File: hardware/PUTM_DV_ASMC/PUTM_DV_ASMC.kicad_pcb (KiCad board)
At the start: 4 copper layers, 100 x 60 mm, 182 parts, among them IC1 BTS722204ESAXUMA1, IC2 BTS722204ESAXUMA1, J1 FTSH-107-01-L-D-K, J2 IPBS-110-01-XX-D-GP, J3 Conn_01x01_Socket, J4 74650073R, Q1 30V/5A, Q2 BUK6D210, Q3 BUK6D210, Q4 BUK6D210, Q5 BUK6D210, T1 TP_VCC, T2 TP_+5V, T3 TP_+3V3, T4 TP_GND, T5 TP_GND, T6 TP_VCC, T7 TP_GND, T8 TP_+5V, T9 TP_GND, U1 LM4040C33FTA, U2 STM32G484RETx, U3 LM1117-3.3, U4 TPS54202HDDCR, U5 ADM3057ExRW, U6 ADM3057ExRW, U7 TLP291-4, Y1 ATX-11-F-32.000MHZ-F05-T

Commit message: make function section
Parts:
- moved TP6 238.4 mm to (276.2, 70.0)
- moved TP7 238.4 mm to (276.2, 73.0)
- moved TP1 219.3 mm to (268.9, 71.8)
- moved C66 156.9 mm to (178.9, 124.3), turned to 90 degrees
- moved D1 155.3 mm to (185.3, 114.2)
- moved D2 154.9 mm to (185.3, 115.9)
- moved D3 154.6 mm to (185.3, 117.7)
- moved D4 154.2 mm to (185.3, 119.5)
- moved C1 153.8 mm to (170.8, 125.2), turned to 180 degrees
- moved R2 152.5 mm to (181.5, 114.1)
- moved C64 152.3 mm to (177.4, 110.0)
- moved R3 152.1 mm to (181.5, 115.8), turned to 180 degrees
- moved C65 152.0 mm to (177.3, 111.7)
- moved R4 151.9 mm to (181.5, 117.7), turned to 180 degrees
- moved C69 151.8 mm to (176.1, 125.2)
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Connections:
- J2 pad 11: /Connectors/OUT_LIDAR -> /Connectors/OUT_RES
- J2 pad 12: /Connectors/OUT_LIDAR -> /Connectors/OUT_EBS
- J2 pad 15: /Connectors/OUT_RES -> /Connectors/OUT_LIDAR
- J2 pad 16: /Connectors/OUT_EBS -> /Connectors/OUT_LIDAR
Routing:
- net +BATT: track 0.00 -> 23.4 mm
- net GND: track 0.00 -> 18.7 mm, vias 0 -> 20
- net /DV_power_supply/Odrive_power_supply/IN0: track 0.00 -> 17.5 mm
- net /DV_power_supply/Dv_power_supply_component/IN0: track 0.00 -> 17.2 mm
- net /DV_power_supply/Odrive_power_supply/IN1: track 0.00 -> 15.2 mm
- net /DV_power_supply/Dv_power_supply_component/IN1: track 0.00 -> 14.5 mm
- net /DV_power_supply/Odrive_power_supply/IN2: track 0.00 -> 13.2 mm
- net /DV_power_supply/Dv_power_supply_component/IN2: track 0.00 -> 12.5 mm
- net /DV_power_supply/Odrive_power_supply/IN3: track 0.66 -> 11.8 mm
- net /DV_power_supply/Odrive_power_supply/SO: track 0.00 -> 10.9 mm
- net /DV_power_supply/Odrive_power_supply/VDD: track 0.00 -> 10.7 mm
- net /DV_power_supply/Dv_power_supply_component/SO: track 0.00 -> 10.7 mm
- net /DV_power_supply/Dv_power_supply_component/IN3: track 0.00 -> 10.6 mm
- net /DV_power_supply/Dv_power_supply_component/SCLK: track 0.00 -> 10.4 mm
- net /DV_power_supply/Dv_power_supply_component/IS: track 0.00 -> 10.4 mm
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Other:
- board outline removed

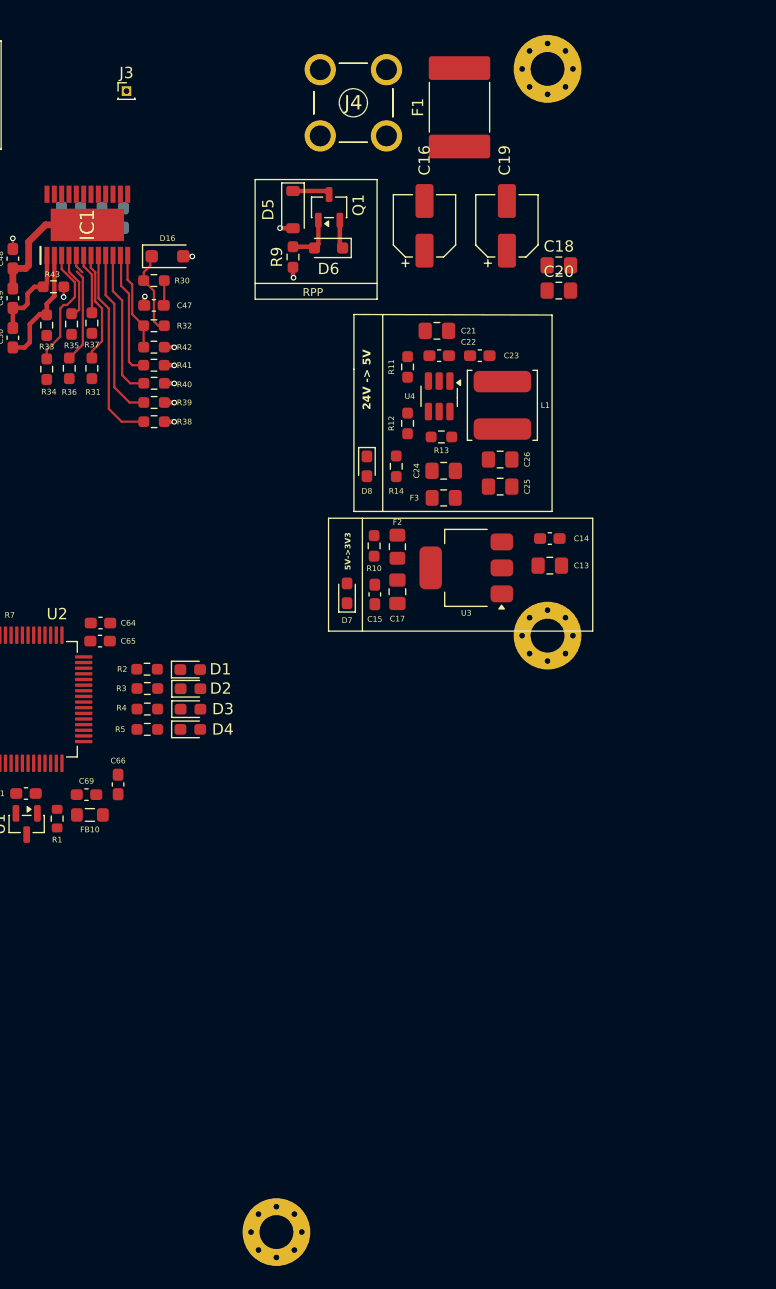
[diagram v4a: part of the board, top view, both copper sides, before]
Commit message: update pins mcu
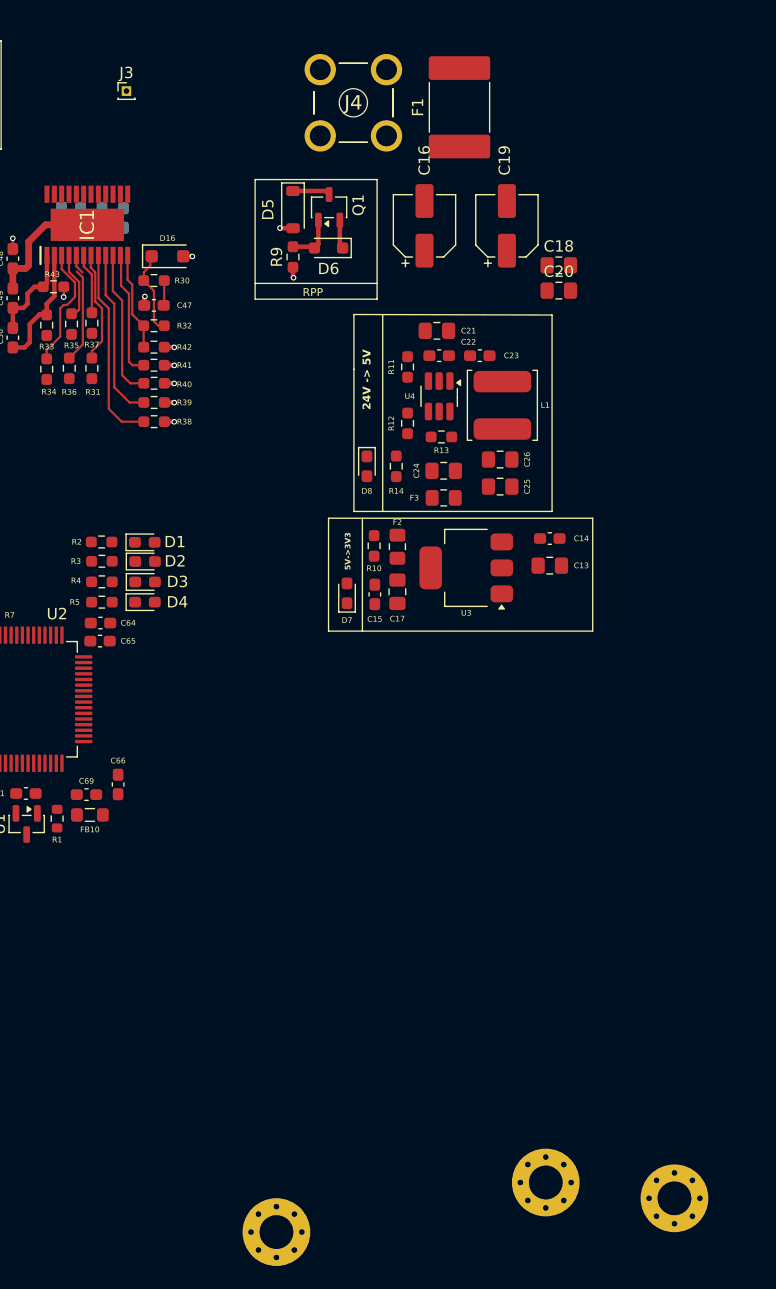
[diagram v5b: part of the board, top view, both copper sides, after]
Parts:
- moved REF** 98.6 mm to (216.8, 159.6)
- moved REF** 51.1 mm to (228.2, 161.0)
- moved D2 12.0 mm to (181.3, 104.6)
- moved D3 12.0 mm to (181.3, 106.4)
- moved D1 12.0 mm to (181.3, 102.9)
- moved R2 12.0 mm to (177.5, 102.9)
- moved D4 12.0 mm to (181.3, 108.2)
- moved R3 12.0 mm to (177.5, 104.6)
- moved R4 12.0 mm to (177.5, 106.4)
- moved R5 12.0 mm to (177.5, 108.2)
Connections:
- U2 pad 33: /ASIS/ASSI_DI_PIN -> unconnected-(U2-PB11-Pad33)
- U2 pad 38: unconnected-(U2-PC6-Pad38) -> /ASIS/ASSI_DO_PIN
- U2 pad 39: unconnected-(U2-PC7-Pad39) -> /ASIS/ASSI_DI_PIN
- U2 pad 51: unconnected-(U2-PA15-Pad51) -> /Microcontroller/DEBUG_LED_1
- U2 pad 52: unconnected-(U2-PC10-Pad52) -> /Microcontroller/DEBUG_LED_4
- U2 pad 53: unconnected-(U2-PC11-Pad53) -> /Microcontroller/DEBUG_LED_3
- U2 pad 54: unconnected-(U2-PC12-Pad54) -> /Microcontroller/DEBUG_LED_2
- U2 pad 57: /Microcontroller/DEBUG_LED_1 -> unconnected-(U2-PB4-Pad57)
- U2 pad 58: /Microcontroller/DEBUG_LED_2 -> unconnected-(U2-PB5-Pad58)
- U2 pad 59: /Microcontroller/DEBUG_LED_3 -> unconnected-(U2-PB6-Pad59)
- U2 pad 60: /Microcontroller/DEBUG_LED_4 -> unconnected-(U2-PB7-Pad60)
- U2 pad 62: /ASIS/ASSI_DO_PIN -> unconnected-(U2-PB9-Pad62)
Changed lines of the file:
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@@
 			(layers "F.Cu" "F.Mask" "F.Paste")
 			(roundrect_rratio 0.25)
-			(net "/ASIS/ASSI_DI_PIN")
+			(net "unconnected-(U2-PB11-Pad33)")
 			(pinfunction "PB11_33")
-			(pintype "bidirectional")
+			(pintype "bidirectional+no_connect")
 		)
 		(pad "34" smd roundrect
@@
 			(layers "F.Cu" "F.Mask" "F.Paste")
 			(roundrect_rratio 0.25)
-			(net "unconnected-(U2-PC6-Pad38)")
+			(net "/ASIS/ASSI_DO_PIN")
 			(pinfunction "PC6_38")
-			(pintype "bidirectional+no_connect")
+			(pintype "bidirectional")
 		)
 		(pad "39" smd roundrect
@@
 			(layers "F.Cu" "F.Mask" "F.Paste")
 			(roundrect_rratio 0.25)
-			(net "unconnected-(U2-PC7-Pad39)")
+			(net "/ASIS/ASSI_DI_PIN")
 			(pinfunction "PC7_39")
-			(pintype "bidirectional+no_connect")
+			(pintype "bidirectional")
 		)
 		(pad "40" smd roundrect
@@
 			(layers "F.Cu" "F.Mask" "F.Paste")
 			(roundrect_rratio 0.25)
-			(net "unconnected-(U2-PA15-Pad51)")
+			(net "/Microcontroller/DEBUG_LED_1")
 			(pinfunction "PA15_51")
-			(pintype "bidirectional+no_connect")
+			(pintype "bidirectional")
 		)
 		(pad "52" smd roundrect
@@
 			(layers "F.Cu" "F.Mask" "F.Paste")
 			(roundrect_rratio 0.25)
-			(net "unconnected-(U2-PC10-Pad52)")
+			(net "/Microcontroller/DEBUG_LED_4")
 			(pinfunction "PC10_52")
-			(pintype "bidirectional+no_connect")
+			(pintype "bidirectional")
 		)
 		(pad "53" smd roundrect
@@
 			(layers "F.Cu" "F.Mask" "F.Paste")
 			(roundrect_rratio 0.25)
-			(net "unconnected-(U2-PC11-Pad53)")
+			(net "/Microcontroller/DEBUG_LED_3")
 			(pinfunction "PC11_53")
-			(pintype "bidirectional+no_connect")
+			(pintype "bidirectional")
 		)
 		(pad "54" smd roundrect
@@
 			(layers "F.Cu" "F.Mask" "F.Paste")
 			(roundrect_rratio 0.25)
-			(net "unconnected-(U2-PC12-Pad54)")
+			(net "/Microcontroller/DEBUG_LED_2")
 			(pinfunction "PC12_54")
-			(pintype "bidirectional+no_connect")
+			(pintype "bidirectional")
 		)
 		(pad "55" smd roundrect
@@
 			(layers "F.Cu" "F.Mask" "F.Paste")
 			(roundrect_rratio 0.25)
-			(net "/Microcontroller/DEBUG_LED_1")
+			(net "unconnected-(U2-PB4-Pad57)")
 			(pinfunction "PB4_57")
-			(pintype "bidirectional")
+			(pintype "bidirectional+no_connect")
 		)
 		(pad "58" smd roundrect
@@
 			(layers "F.Cu" "F.Mask" "F.Paste")
 			(roundrect_rratio 0.25)
-			(net "/Microcontroller/DEBUG_LED_2")
+			(net "unconnected-(U2-PB5-Pad58)")
 			(pinfunction "PB5_58")
-			(pintype "bidirectional")
+			(pintype "bidirectional+no_connect")
 		)
 		(pad "59" smd roundrect
@@
 			(layers "F.Cu" "F.Mask" "F.Paste")
 			(roundrect_rratio 0.25)
-			(net "/Microcontroller/DEBUG_LED_3")
+			(net "unconnected-(U2-PB6-Pad59)")
 			(pinfunction "PB6_59")
-			(pintype "bidirectional")
+			(pintype "bidirectional+no_connect")
 		)
 		(pad "60" smd roundrect
@@
 			(layers "F.Cu" "F.Mask" "F.Paste")
 			(roundrect_rratio 0.25)
-			(net "/Microcontroller/DEBUG_LED_4")
+			(net "unconnected-(U2-PB7-Pad60)")
 			(pinfunction "PB7_60")
-			(pintype "bidirectional")
+			(pintype "bidirectional+no_connect")
 		)
 		(pad "61" smd roundrect
@@
 			(layers "F.Cu" "F.Mask" "F.Paste")
 			(roundrect_rratio 0.25)
-			(net "/ASIS/ASSI_DO_PIN")
+			(net "unconnected-(U2-PB9-Pad62)")
 			(pinfunction "PB9_62")
-			(pintype "bidirectional")
+			(pintype "bidirectional+no_connect")
 		)
 		(pad "63" smd roundrect
@@
 	(footprint "Resistor_SMD:R_0603_1608Metric_Pad0.98x0.95mm_HandSolder"
 		(layer "F.Cu")
-		(at 181.5125 117.67 180)
+		(at 177.4875 106.4 180)
 		(descr "Resistor SMD 0603 (1608 Metric), square (rectangular) end terminal, IPC-7351 nominal with elongated pad for handsoldering. (Body size source: IPC-SM-782 page 72, https://www.pcb-3d.com/wordpress/wp-content/uploads/ipc-sm-782a_amendment_1_and_2.pdf)")
 		(tags "resistor handsolder")
@@
 	(footprint "LED_SMD:LED_0603_1608Metric_Pad1.05x0.95mm_HandSolder"
 		(layer "F.Cu")
-		(at 185.3125 114.17)
+		(at 181.2875 102.9)
 		(descr "LED SMD 0603 (1608 Metric), square (rectangular) end terminal, IPC-7351 nominal, (Body size source: http://www.tortai-tech.com/upload/download/2011102023233369053.pdf)")
 		(tags "LED handsolder")
@@
 	(footprint "LED_SMD:LED_0603_1608Metric_Pad1.05x0.95mm_HandSolder"
 		(layer "F.Cu")
-		(at 185.325 119.47)
+		(at 181.3 108.2)
 		(descr "LED SMD 0603 (1608 Metric), square (rectangular) end terminal, IPC-7351 nominal, (Body size source: http://www.tortai-tech.com/upload/download/2011102023233369053.pdf)")
 		(tags "LED handsolder")
@@
 	(footprint "MountingHole:MountingHole_3mm_Pad_Via"
 		(layer "F.Cu")
-		(at 216.965 111.165)
+		(at 228.20901 161.00901)
 		(descr "Mounting Hole 3mm")
 		(tags "mounting hole 3mm")
@@
 	(footprint "Resistor_SMD:R_0603_1608Metric_Pad0.98x0.95mm_HandSolder"
 		(layer "F.Cu")
-		(at 181.4875 114.14)
+		(at 177.4625 102.87)
 		(descr "Resistor SMD 0603 (1608 Metric), square (rectangular) end terminal, IPC-7351 nominal with elongated pad for handsoldering. (Body size source: IPC-SM-782 page 72, https://www.pcb-3d.com/wordpress/wp-content/uploads/ipc-sm-782a_amendment_1_and_2.pdf)")
 		(tags "resistor handsolder")
@@
 	(footprint "Resistor_SMD:R_0603_1608Metric_Pad0.98x0.95mm_HandSolder"
 		(layer "F.Cu")
-		(at 181.5125 119.47 180)
+		(at 177.4875 108.2 180)
 		(descr "Resistor SMD 0603 (1608 Metric), square (rectangular) end terminal, IPC-7351 nominal with elongated pad for handsoldering. (Body size source: IPC-SM-782 page 72, https://www.pcb-3d.com/wordpress/wp-content/uploads/ipc-sm-782a_amendment_1_and_2.pdf)")
 		(tags "resistor handsolder")
@@
 	(footprint "MountingHole:MountingHole_3mm_Pad_Via"
 		(layer "F.Cu")
-		(at 216.965 60.965)
+		(at 216.80901 159.60901)
 		(descr "Mounting Hole 3mm")
 		(tags "mounting hole 3mm")
@@
 	(footprint "LED_SMD:LED_0603_1608Metric_Pad1.05x0.95mm_HandSolder"
 		(layer "F.Cu")
-		(at 185.3375 115.87)
+		(at 181.3125 104.6)
 		(descr "LED SMD 0603 (1608 Metric), square (rectangular) end terminal, IPC-7351 nominal, (Body size source: http://www.tortai-tech.com/upload/download/2011102023233369053.pdf)")
 		(tags "LED handsolder")
@@
 	(footprint "Resistor_SMD:R_0603_1608Metric_Pad0.98x0.95mm_HandSolder"
 		(layer "F.Cu")
-		(at 181.5125 115.85 180)
+		(at 177.4875 104.58 180)
 		(descr "Resistor SMD 0603 (1608 Metric), square (rectangular) end terminal, IPC-7351 nominal with elongated pad for handsoldering. (Body size source: IPC-SM-782 page 72, https://www.pcb-3d.com/wordpress/wp-content/uploads/ipc-sm-782a_amendment_1_and_2.pdf)")
 		(tags "resistor handsolder")
@@
 	(footprint "LED_SMD:LED_0603_1608Metric_Pad1.05x0.95mm_HandSolder"
 		(layer "F.Cu")
-		(at 185.3375 117.68)
+		(at 181.3125 106.41)
 		(descr "LED SMD 0603 (1608 Metric), square (rectangular) end terminal, IPC-7351 nominal, (Body size source: http://www.tortai-tech.com/upload/download/2011102023233369053.pdf)")
 		(tags "LED handsolder")

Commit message: make zones
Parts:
- removed J3: Conn_01x01_Socket, Connector_PinHeader_1.00mm:PinHeader_1x01_P1.00mm_Vertical
- removed the REF** at (228.2, 161.0)
- removed U7: TLP291-4, Package_SO:SOIC-16_4.55x10.3mm_P1.27mm
- added D9: LED, LED_SMD:LED_0603_1608Metric_Pad1.05x0.95mm_HandSolder, F.Cu at (134.6, 48.2)
- added J5: 74650073R, 74650073R:74650073R, F.Cu at (175.4, 30.3)
- added K2: FINDER-32.21-x000, Relay_THT:Relay_SPDT_Finder_32.21-x000, F.Cu at (138.6, 42.6)
- added U14: FODM217B, Package_SO:SOP-4_4.4x2.6mm_P1.27mm, F.Cu at (141.0, 79.2)
- added U15: FODM217B, Package_SO:SOP-4_4.4x2.6mm_P1.27mm, F.Cu at (141.2, 84.6)
- D10: value SMBJ30A -> D_Small; footprint Diode_SMD:D_SMB_Handsoldering -> Diode_SMD:D_0805_2012Metric_Pad1.15x1.40mm_HandSolder
- moved REF** 152.2 mm to (125.3, 67.4)
- moved REF** 133.4 mm to (205.3, 26.7)
- moved J1 104.4 mm to (182.1, 74.6)
- moved D13 103.5 mm to (180.5, 81.0)
- moved TP2 102.7 mm to (233.2, 71.6)
- moved C34 97.5 mm to (181.9, 109.7)
- moved C30 97.4 mm to (172.8, 100.1)
- moved C37 97.4 mm to (196.1, 103.9)
- moved C38 97.4 mm to (189.6, 104.0)
- moved D11 97.4 mm to (168.8, 97.8)
- moved FB5 97.4 mm to (170.8, 105.5)
- moved FB9 97.4 mm to (192.3, 98.3)
- moved C33 97.4 mm to (167.4, 104.4)
- moved C41 97.4 mm to (194.4, 98.3)
- moved FB4 97.4 mm to (170.8, 103.6)
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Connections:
- REF** pad 1: (no net) -> GND (x3)
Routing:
- net /Power_supply/RPP_G: track 4.55 -> 0.00 mm
- net /Power_supply/RPP_D: track 3.33 -> 0.00 mm
- net +24V: track 2.57 -> 0.00 mm
- net GND: track 18.7 -> 16.6 mm, vias 20 -> 18
- added copper zone on B.Cu, net +3.3V
- added copper zone on F.Cu, net +5V
- added copper zone on In1.Cu, net GND
- added copper zone on In2.Cu, net GND
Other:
- board outline added: 90.4 x 95 mm
- board text added: "ASSI"
- board text added: "SAFETY SENSE"

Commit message: work on supply and zones
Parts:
- moved T2 51.2 mm to (192.0, 75.0)
- moved T3 39.5 mm to (207.5, 85.9)
- moved T6 37.0 mm to (201.4, 55.0)
- moved Q4 7.75 mm to (143.3, 64.7)
- moved R26 7.75 mm to (142.3, 67.5)
- moved R27 7.75 mm to (144.5, 67.5)
- moved REF** 7.47 mm to (132.7, 66.4)
- moved REF** 7.00 mm to (205.5, 102.7)
- moved J5 5.74 mm to (181.1, 30.3), turned to 90 degrees
- moved C18 5.31 mm to (202.5, 48.9)
- moved C20 5.31 mm to (202.5, 51.1)
- moved Q2 4.98 mm to (146.9, 64.5)
- moved R22 4.98 mm to (146.3, 67.6)
- moved R24 4.98 mm to (148.1, 67.6)
- moved D8 4.94 mm to (192.0, 70.3)
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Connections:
- C3 pad 1: +3.3V -> +3V3
- C41 pad 1: +3.3V -> +3V3
- C43 pad 1: +3.3V -> +3V3
- C47 pad 1: /DV_power_supply/Odrive_power_supply/FUSE_IS0 -> /DV_power_supply/FUSE_IS0
- C51 pad 1: /DV_power_supply/Odrive_power_supply/ODRIVE_1 -> /Connectors/ODRIVE4
- C52 pad 1: /DV_power_supply/Odrive_power_supply/ODRIVE_2 -> /Connectors/ODRIVE4
- C53 pad 1: /DV_power_supply/Odrive_power_supply/ODRIVE_3 -> /Connectors/ODRIVE4
- C54 pad 1: /DV_power_supply/Odrive_power_supply/ODRIVE_4 -> /Connectors/ODRIVE4
- C55 pad 1: /DV_power_supply/Dv_power_supply_component/FUSE_IS1 -> /DV_power_supply/FUSE_IS1
- C63 pad 1: +3.3V -> +3V3
- C64 pad 1: +3.3V -> +3V3
- C65 pad 1: +3.3V -> +3V3
- C66 pad 1: +3.3V -> +3V3
- C67 pad 1: +3.3V -> +3V3
- C68 pad 1: +3.3V -> +3V3
- D1 pad 2: +3.3V -> +3V3
- D2 pad 2: +3.3V -> +3V3
- D3 pad 2: +3.3V -> +3V3
- D4 pad 2: +3.3V -> +3V3
- D9 pad 1: Net-(D10-A) -> GND
- FB10 pad 1: +3.3V -> +3V3
- FB8 pad 2: +3.3V -> +3V3
- FB9 pad 2: +3.3V -> +3V3
- IC1 pad 13: /DV_power_supply/Odrive_power_supply/ODRIVE_4 -> /Connectors/ODRIVE4
- IC1 pad 14: /DV_power_supply/Odrive_power_supply/ODRIVE_4 -> /Connectors/ODRIVE4
- IC1 pad 15: /DV_power_supply/Odrive_power_supply/ODRIVE_4 -> /Connectors/ODRIVE4
- IC1 pad 16: /DV_power_supply/Odrive_power_supply/ODRIVE_4 -> /Connectors/ODRIVE4
- IC1 pad 17: /DV_power_supply/Odrive_power_supply/ODRIVE_3 -> /Connectors/ODRIVE4
- IC1 pad 18: /DV_power_supply/Odrive_power_supply/ODRIVE_3 -> /Connectors/ODRIVE4
- IC1 pad 19: /DV_power_supply/Odrive_power_supply/ODRIVE_2 -> /Connectors/ODRIVE4
- IC1 pad 20: /DV_power_supply/Odrive_power_supply/ODRIVE_2 -> /Connectors/ODRIVE4
- IC1 pad 21: /DV_power_supply/Odrive_power_supply/ODRIVE_1 -> /Connectors/ODRIVE4
- IC1 pad 22: /DV_power_supply/Odrive_power_supply/ODRIVE_1 -> /Connectors/ODRIVE4
- IC1 pad 23: /DV_power_supply/Odrive_power_supply/ODRIVE_1 -> /Connectors/ODRIVE4
- IC1 pad 24: /DV_power_supply/Odrive_power_supply/ODRIVE_1 -> /Connectors/ODRIVE4
- J5 pad 1: /Connectors/ODRIVE_4 -> /Connectors/ODRIVE4
- J5 pad 2: /Connectors/ODRIVE_1 -> /Connectors/ODRIVE4
- J5 pad 3: /Connectors/ODRIVE_2 -> /Connectors/ODRIVE4
- J5 pad 4: /Connectors/ODRIVE_3 -> /Connectors/ODRIVE4
- R19 pad 1: +3.3V -> +3V3
- R20 pad 1: +3.3V -> +3V3
- R21 pad 1: +BATT -> /Connectors/RES_SAFETY_OUTPUT
- R30 pad 1: /DV_power_supply/Odrive_power_supply/FUSE_IS0 -> /DV_power_supply/FUSE_IS0
- R31 pad 1: /DV_power_supply/LHI.0 -> /DV_power_supply/LHI0
- R34 pad 1: /DV_power_supply/SPI.MISO -> /DV_power_supply/SPI1.MISO
- R35 pad 1: /DV_power_supply/SPI.MOSI -> /DV_power_supply/SPI1.MOSI
- R36 pad 1: /DV_power_supply/SPI.SCK -> /DV_power_supply/SPI1.SCK
- R37 pad 1: /DV_power_supply/SPI.NSS -> /DV_power_supply/SPI1.NSS
- R44 pad 1: /DV_power_supply/Dv_power_supply_component/FUSE_IS1 -> /DV_power_supply/FUSE_IS1
- R45 pad 1: /DV_power_supply/LHI.1 -> /DV_power_supply/LHI1
- R48 pad 1: /DV_power_supply/SPI.MISO -> /DV_power_supply/SPI1.MISO
- R49 pad 1: /DV_power_supply/SPI.MOSI -> /DV_power_supply/SPI1.MOSI
- R50 pad 1: /DV_power_supply/SPI.SCK -> /DV_power_supply/SPI1.SCK
- R51 pad 1: /DV_power_supply/SPI.NSS -> /DV_power_supply/SPI1.NSS
- R6 pad 1: +3.3V -> +3V3
- R7 pad 1: +3.3V -> +3V3
- U2 pad 1: +3.3V -> +3V3
- U2 pad 12: /Microcontroller/LHI.0 -> /DV_power_supply/LHI0
- U2 pad 13: /Microcontroller/LHI.1 -> /DV_power_supply/LHI1
- U2 pad 16: +3.3V -> +3V3
- U2 pad 19: /Microcontroller/SPI1_SCK -> /DV_power_supply/SPI1.SCK
- U2 pad 20: /Microcontroller/SPI1_MISO -> /DV_power_supply/SPI1.MISO
- U2 pad 21: /Microcontroller/SPI1_MOSI -> /DV_power_supply/SPI1.MOSI
- U2 pad 32: +3.3V -> +3V3
- U2 pad 40: /Microcontroller/FUSE_ISO.0 -> /DV_power_supply/FUSE_IS0
- U2 pad 41: /Microcontroller/FUSE_ISO.1 -> /DV_power_supply/FUSE_IS1
- U2 pad 42: /Microcontroller/SPI1_NSS -> /DV_power_supply/SPI1.NSS
- U2 pad 48: +3.3V -> +3V3
- U2 pad 64: +3.3V -> +3V3
- Y1 pad 4: +3.3V -> +3V3
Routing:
- net GND: track 16.6 -> 89.5 mm, vias 18 -> 100
- net +3V3: track 0.00 -> 42.1 mm, vias 0 -> 17
- net /DV_power_supply/SPI1.MISO: track 0.00 -> 27.4 mm
- net /DV_power_supply/SPI1.SCK: track 0.00 -> 26.4 mm, vias 0 -> 2
- net +BATT: track 23.4 -> 42.6 mm
- net /Power_supply/VO_+3.3V: track 0.00 -> 9.03 mm
- net /Connectors/SWCLK: track 0.00 -> 8.67 mm
- net /Connectors/SWO: track 0.00 -> 8.38 mm
- net /Power_supply/SW_+5V: track 0.00 -> 8.25 mm
- net /Connectors/SWDIO: track 0.00 -> 6.91 mm
- net +3.3VA: track 0.00 -> 6.81 mm
- net /Microcontroller/NRST: track 0.00 -> 6.62 mm
- net /Microcontroller/VREF: track 0.00 -> 6.53 mm
- net /DV_power_supply/LHI0: track 0.00 -> 6.47 mm
- net /Connectors/NRST: track 0.00 -> 6.47 mm
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- added copper zone on F.Cu, net +24V
- added copper zone on In1.Cu, net +24V
- added copper zone on In2.Cu, net +24V
- added copper zone on B.Cu, net +3V3
- added copper zone on In1.Cu, net +5V
- added copper zone on In2.Cu, net +5V
- added copper zone on F.Cu, net +BATT
- added copper zone on In1.Cu, net +BATT
- added copper zone on In2.Cu, net +BATT
- added copper zone on F.Cu, net /Connectors/ODRIVE4
- added copper zone on In1.Cu, net /Connectors/ODRIVE4
- added copper zone on In2.Cu, net /Connectors/ODRIVE4
- added copper zone on F.Cu, net /Connectors/OUT_ASSI
- added copper zone on In1.Cu, net /Connectors/OUT_ASSI
- added copper zone on In2.Cu, net /Connectors/OUT_ASSI
- added copper zone on F.Cu, net /Connectors/OUT_EBS
- added copper zone on In1.Cu, net /Connectors/OUT_EBS
- added copper zone on In2.Cu, net /Connectors/OUT_EBS
- added copper zone on F.Cu, net /Connectors/OUT_LIDAR
- added copper zone on In1.Cu, net /Connectors/OUT_LIDAR
- added copper zone on In2.Cu, net /Connectors/OUT_LIDAR
- added copper zone on F.Cu, net /Connectors/OUT_RES
- added copper zone on In1.Cu, net /Connectors/OUT_RES
- added copper zone on In2.Cu, net /Connectors/OUT_RES
- added copper zone on F.Cu, net /Power_supply/+5V_OUT
- added copper zone on In1.Cu, net /Power_supply/+5V_OUT
- added copper zone on In2.Cu, net /Power_supply/+5V_OUT
- added copper zone on F.Cu, net /Power_supply/RPP_D
- added copper zone on In1.Cu, net /Power_supply/RPP_D
- added copper zone on In2.Cu, net /Power_supply/RPP_D
- added copper zone on F.Cu, net /Power_supply/VO_+3.3V
- added copper zone on In1.Cu, net /Power_supply/VO_+3.3V
- added copper zone on In2.Cu, net /Power_supply/VO_+3.3V
- added copper zone on B.Cu, net GND
- added copper zone on F.Cu, net GND
- removed copper zone on B.Cu, net +3.3V
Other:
- board size 90.4 x 95 mm -> 88.4 x 88.2 mm
- board text added: "ASSI & BUZZER"
- board text removed: "ASSI"
